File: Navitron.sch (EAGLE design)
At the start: 85 parts, among them J2 DX07S016JA1R1500, Q1 ROHM_RUM002N02T2LROHM_RUM002N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, Q2 2.5A/30V, Q3 ROHM_RUM002N02T2LROHM_RUM002N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, Q4 ROHM_RUM002N02T2LROHM_RUM002N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, Q5 ROHM_RUM002N02T2LROHM_RUM002N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, T1 BC847, T2 BC847, U2 9DoF IMU, U3 MCP73831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

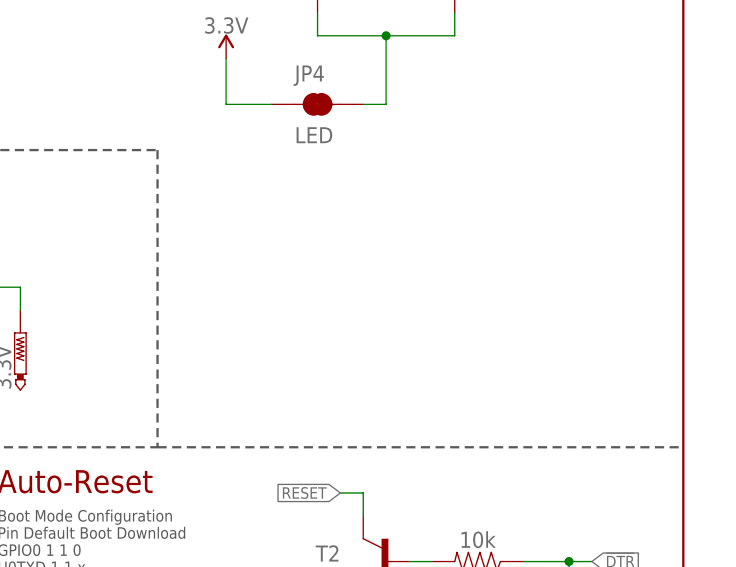
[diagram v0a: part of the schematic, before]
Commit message: fix #1
- Fixed the heatsink, of the ICM-20948 briding the FSYNC and INT lines
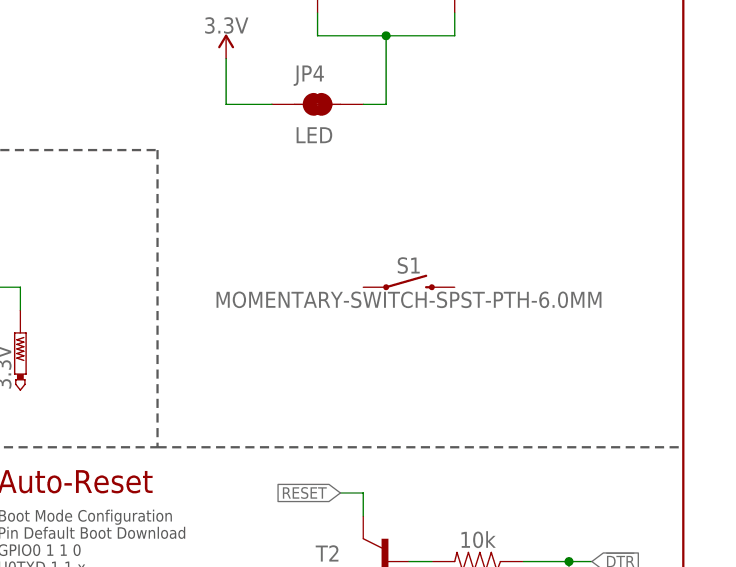
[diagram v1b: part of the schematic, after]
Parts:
- added S1: MOMENTARY-SWITCH-SPST-PTH-6.0MM, SparkFun-Switches:MOMENTARY-SWITCH-SPST-PTH-6.0MM
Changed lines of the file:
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@@
 <part name="GND" library="testpad" library_urn="urn:adsk.eagle:library:385" deviceset="PTR1" device="B1,27" package3d_urn="urn:adsk.eagle:package:27944/2"/>
 <part name="3.3V" library="testpad" library_urn="urn:adsk.eagle:library:385" deviceset="PTR1" device="B1,27" package3d_urn="urn:adsk.eagle:package:27944/2"/>
+<part name="S1" library="SparkFun-Switches" library_urn="urn:adsk.eagle:library:535" deviceset="MOMENTARY-SWITCH-SPST" device="-PTH-6.0MM" package3d_urn="urn:adsk.eagle:package:40163/1"/>
 </parts>
 <sheets>
@@
 <attribute name="TP_SIGNAL_NAME" x="176.53" y="86.36" size="1.778" layer="97"/>
 </instance>
+<instance part="S1" gate="G$1" x="218.44" y="93.98" smashed="yes">
+<attribute name="NAME" x="218.44" y="95.504" size="1.778" layer="95" font="vector" align="bottom-center"/>
+<attribute name="VALUE" x="218.44" y="93.472" size="1.778" layer="96" font="vector" align="top-center"/>
+</instance>
 </instances>

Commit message: Remove Temporary Button
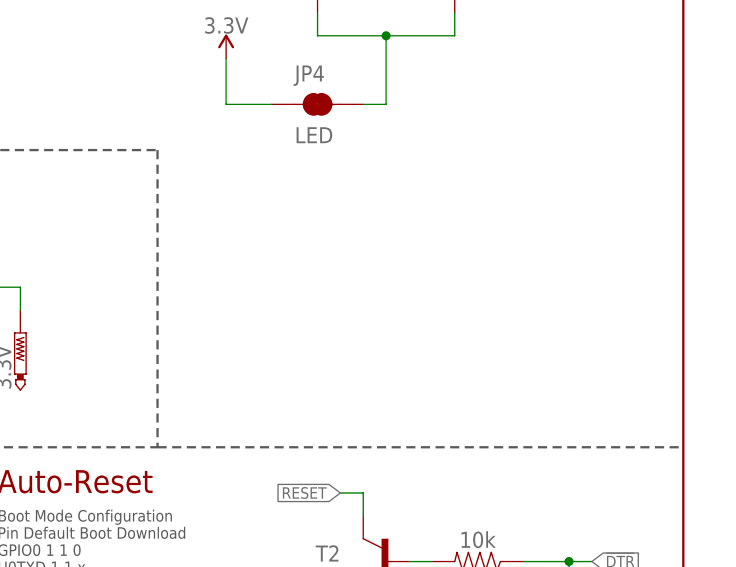
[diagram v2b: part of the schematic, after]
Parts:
- removed S1: MOMENTARY-SWITCH-SPST-PTH-6.0MM, SparkFun-Switches:MOMENTARY-SWITCH-SPST-PTH-6.0MM
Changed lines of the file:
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@@
 <part name="GND" library="testpad" library_urn="urn:adsk.eagle:library:385" deviceset="PTR1" device="B1,27" package3d_urn="urn:adsk.eagle:package:27944/2"/>
 <part name="3.3V" library="testpad" library_urn="urn:adsk.eagle:library:385" deviceset="PTR1" device="B1,27" package3d_urn="urn:adsk.eagle:package:27944/2"/>
-<part name="S1" library="SparkFun-Switches" library_urn="urn:adsk.eagle:library:535" deviceset="MOMENTARY-SWITCH-SPST" device="-PTH-6.0MM" package3d_urn="urn:adsk.eagle:package:40163/1"/>
 </parts>
 <sheets>
@@
 <attribute name="TP_SIGNAL_NAME" x="176.53" y="86.36" size="1.778" layer="97"/>
 </instance>
-<instance part="S1" gate="G$1" x="218.44" y="93.98" smashed="yes">
-<attribute name="NAME" x="218.44" y="95.504" size="1.778" layer="95" font="vector" align="bottom-center"/>
-<attribute name="VALUE" x="218.44" y="93.472" size="1.778" layer="96" font="vector" align="top-center"/>
-</instance>
 </instances>
